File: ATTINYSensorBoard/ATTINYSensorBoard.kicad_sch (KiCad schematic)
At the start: 17 parts, among them J1 ICSP, J2 POWER/CAN, U1 ATtiny841-SS, U2 MCP25625-x-SS, U3 74HC04

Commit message: Finished Sensor Board Template
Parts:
- added J3: Conn_01x04, Connector_PinHeader_2.54mm:PinHeader_1x04_P2.54mm_Vertical, symbol Connector_Generic:Conn_01x04
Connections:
- net USER0: now also J3.1 (Pin_1)
- net USER1: now also J3.2 (Pin_2)
- net USER2: now also J3.3 (Pin_3)
- net USER3: now also J3.4 (Pin_4)
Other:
- company: Pack Motorsports Baja -> ©️ 2024 Pack Motorsports Baja
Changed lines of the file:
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@@
 	(title_block
 		(title "ATtiny Senor Board Template")
-		(date "2024-10-03")
+		(date "2024-10-17")
 		(rev "1")
-		(company "Pack Motorsports Baja")
-		(comment 1 "©️ 2024 Pack Motorsports")
+		(company "©️ 2024 Pack Motorsports Baja")
 	)
 	(junction
@@
 	(wire
 		(pts
-			(xy 127 88.9) (xy 127 71.12)
+			(xy 127 88.9) (xy 127 69.85)
 		)
 		(stroke
@@
 	(wire
 		(pts
-			(xy 125.73 68.58) (xy 125.73 86.36)
+			(xy 125.73 67.31) (xy 125.73 86.36)
 		)
 		(stroke
@@
 		)
 	)
+	(polyline
+		(pts
+			(xy 139.7 59.055) (xy 139.7 62.23)
+		)
+		(stroke
+			(width 0)
+			(type default)
+		)
+	)
 	(wire
 		(pts
@@
 		)
 	)
+	(polyline
+		(pts
+			(xy 136.525 59.055) (xy 139.7 59.055)
+		)
+		(stroke
+			(width 0)
+			(type default)
+		)
+	)
 	(wire
 		(pts
@@
 	(wire
 		(pts
-			(xy 128.27 73.66) (xy 134.62 73.66)
+			(xy 128.27 72.39) (xy 134.62 72.39)
 		)
 		(stroke
@@
 	(wire
 		(pts
-			(xy 125.73 68.58) (xy 134.62 68.58)
+			(xy 125.73 67.31) (xy 134.62 67.31)
 		)
 		(stroke
@@
 	(wire
 		(pts
-			(xy 127 71.12) (xy 134.62 71.12)
+			(xy 127 69.85) (xy 134.62 69.85)
 		)
 		(stroke
@@
 		)
 	)
-	(polyline
-		(pts
-			(xy 135.89 63.5) (xy 135.89 74.295)
-		)
-		(stroke
-			(width 0)
-			(type default)
-		)
-	)
 	(wire
 		(pts
@@
 	(wire
 		(pts
-			(xy 128.27 91.44) (xy 128.27 73.66)
+			(xy 128.27 91.44) (xy 128.27 72.39)
 		)
 		(stroke
@@
 		)
 	)
-	(polyline
-		(pts
-			(xy 134.62 63.5) (xy 135.89 63.5)
-		)
-		(stroke
-			(width 0)
-			(type default)
-		)
-	)
 	(wire
 		(pts
@@
 	(wire
 		(pts
-			(xy 124.46 66.04) (xy 124.46 83.82)
-		)
-		(stroke
-			(width 0)
-			(type default)
-		)
-	)
-	(polyline
-		(pts
-			(xy 134.62 74.295) (xy 135.89 74.295)
+			(xy 124.46 64.77) (xy 124.46 83.82)
 		)
 		(stroke
@@
 	(wire
 		(pts
-			(xy 124.46 66.04) (xy 134.62 66.04)
+			(xy 124.46 64.77) (xy 134.62 64.77)
 		)
 		(stroke
@@
 	(text "SENSOR\nINPUTS"
 		(exclude_from_sim no)
-		(at 136.398 69.088 0)
+		(at 128.27 59.182 0)
 		(effects
 			(font
@@
 	)
 	(label "USER2"
-		(at 134.62 71.12 180)
+		(at 134.62 69.85 180)
 		(fields_autoplaced yes)
 		(effects
@@
 	)
 	(label "USER3"
-		(at 134.62 73.66 180)
+		(at 134.62 72.39 180)
 		(fields_autoplaced yes)
 		(effects
@@
 	)
 	(label "USER0"
-		(at 134.62 66.04 180)
+		(at 134.62 64.77 180)
 		(fields_autoplaced yes)
 		(effects
@@
 	)
 	(label "USER1"
-		(at 134.62 68.58 180)
+		(at 134.62 67.31 180)
 		(fields_autoplaced yes)
 		(effects
@@
 					(unit 1)
 				)
+			)
+		)
+	)
+	(symbol
+		(lib_id "Connector_Generic:Conn_01x04")
+		(at 139.7 67.31 0)
+		(unit 1)
+		(exclude_from_sim no)
+		(in_bom yes)
+		(on_board yes)
+		(dnp no)
+		(fields_autoplaced yes)
+		(property "Reference" "J3"
+			(at 142.24 67.3099 0)
+			(effects
+				(font
+					(size 1.27 1.27)
+				)
+				(justify left)
+			)
+		)
+		(property "Value" "Conn_01x04"
+			(at 142.24 69.8499 0)
+			(effects
+				(font
+					(size 1.27 1.27)
+				)
+				(justify left)
+			)
+		)
+		(property "Footprint" "Connector_PinHeader_2.54mm:PinHeader_1x04_P2.54mm_Vertical"
+			(at 139.7 67.31 0)
+			(effects
+				(font
+					(size 1.27 1.27)
+				)
+				(hide yes)
+			)
+		)
+		(property "Datasheet" "~"
+			(at 139.7 67.31 0)
+			(effects
+				(font
+					(size 1.27 1.27)
+				)
+				(hide yes)
+			)
+		)
+		(property "Description" "Generic connector, single row, 01x04, script generated (kicad-library-utils/schlib/autogen/connector/)"
+			(at 139.7 67.31 0)
+			(effects
+				(font
+					(size 1.27 1.27)
+				)
+				(hide yes)
+			)
+		)
+		(pin "3"
+		)
+		(pin "4"
+		)
+		(pin "1"
+		)
+		(pin "2"
+		)
+		(instances
+			(project ""
+				(path "/6c2b8c5e-e617-4dcc-bfbe-6767b59298bb"
+					(reference "J3")
+					(unit 1)
+				)

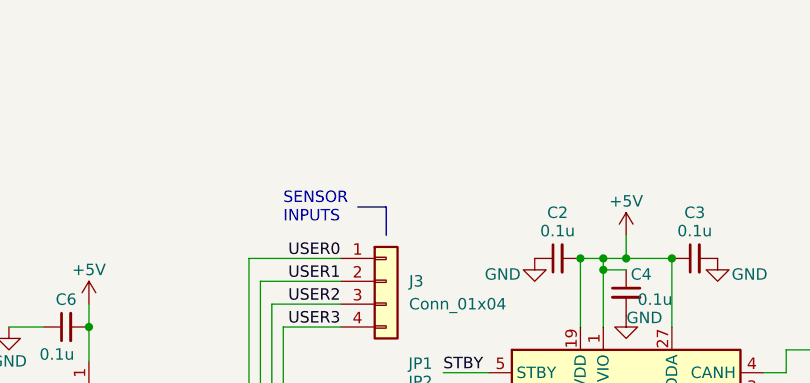
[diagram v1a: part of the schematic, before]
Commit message: Fixed grounds
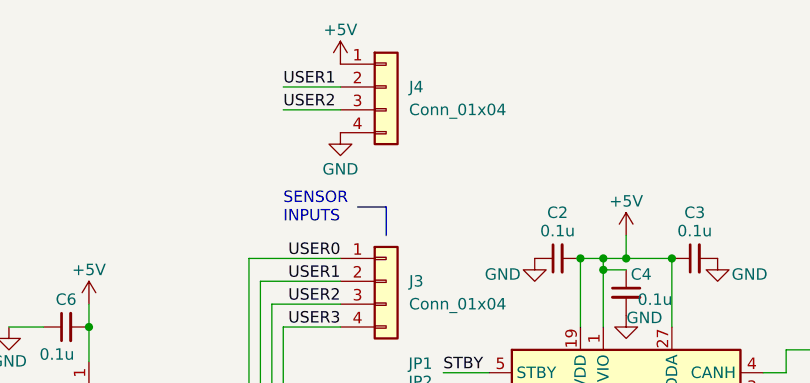
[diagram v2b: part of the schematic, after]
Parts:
- added J4: Conn_01x04, symbol Connector_Generic:Conn_01x04
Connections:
- net +5V: now also J4.1 (Pin_1)
- net GND: now also J4.4 (Pin_4)
- net USER1: now also J4.2 (Pin_2)
- net USER2: now also J4.3 (Pin_3)
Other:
- title: ATtiny Senor Board Template -> ATtiny Sensor Board Template
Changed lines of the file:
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@@
 	(paper "A4")
 	(title_block
-		(title "ATtiny Senor Board Template")
+		(title "ATtiny Sensor Board Template")
 		(date "2024-10-17")
 		(rev "1")
@@
 	(wire
 		(pts
+			(xy 128.27 48.26) (xy 134.62 48.26)
+		)
+		(stroke
+			(width 0)
+			(type default)
+		)
+	)
+	(wire
+		(pts
 			(xy 184.15 85.09) (xy 184.15 95.25)
 		)
@@
 	(wire
 		(pts
+			(xy 128.27 45.72) (xy 134.62 45.72)
+		)
+		(stroke
+			(width 0)
+			(type default)
+		)
+	)
+	(wire
+		(pts
 			(xy 134.62 96.52) (xy 121.92 96.52)
 		)
@@
 		)
 	)
+	(label "USER1"
+		(at 128.27 45.72 0)
+		(fields_autoplaced yes)
+		(effects
+			(font
+				(size 1.27 1.27)
+			)
+			(justify left bottom)
+		)
+	)
 	(label "STBY"
 		(at 146.05 77.47 0)
@@
 		)
 	)
+	(label "USER2"
+		(at 128.27 48.26 0)
+		(fields_autoplaced yes)
+		(effects
+			(font
+				(size 1.27 1.27)
+			)
+			(justify left bottom)
+		)
+	)
 	(symbol
 		(lib_id "power:PWR_FLAG")
@@
 	)
 	(symbol
+		(lib_id "power:+5V")
+		(at 134.62 43.18 0)
+		(unit 1)
+		(exclude_from_sim no)
+		(in_bom yes)
+		(on_board yes)
+		(dnp no)
+		(property "Reference" "#PWR025"
+			(at 134.62 46.99 0)
+			(effects
+				(font
+					(size 1.27 1.27)
+				)
+				(hide yes)
+			)
+		)
+		(property "Value" "+5V"
+			(at 134.62 39.37 0)
+			(effects
+				(font
+					(size 1.27 1.27)
+				)
+			)
+		)
+		(property "Footprint" ""
+			(at 134.62 43.18 0)
+			(effects
+				(font
+					(size 1.27 1.27)
+				)
+				(hide yes)
+			)
+		)
+		(property "Datasheet" ""
+			(at 134.62 43.18 0)
+			(effects
+				(font
+					(size 1.27 1.27)
+				)
+				(hide yes)
+			)
+		)
+		(property "Description" "Power symbol creates a global label with name \"+5V\""
+			(at 134.62 43.18 0)
+			(effects
+				(font
+					(size 1.27 1.27)
+				)
+				(hide yes)
+			)
+		)
+		(pin "1"
+		)
+		(instances
+			(project "ATTINYSensorBoard"
+				(path "/6c2b8c5e-e617-4dcc-bfbe-6767b59298bb"
+					(reference "#PWR025")
+					(unit 1)
+				)
+			)
+		)
+	)
+	(symbol
 		(lib_id "Device:C_Small")
 		(at 158.75 64.77 90)
@@
 	)
 	(symbol
+		(lib_id "power:GND")
+		(at 134.62 50.8 0)
+		(unit 1)
+		(exclude_from_sim no)
+		(in_bom yes)
+		(on_board yes)
+		(dnp no)
+		(property "Reference" "#PWR026"
+			(at 134.62 57.15 0)
+			(effects
+				(font
+					(size 1.27 1.27)
+				)
+				(hide yes)
+			)
+		)
+		(property "Value" "GND"
+			(at 134.62 54.864 0)
+			(effects
+				(font
+					(size 1.27 1.27)
+				)
+			)
+		)
+		(property "Footprint" ""
+			(at 134.62 50.8 0)
+			(effects
+				(font
+					(size 1.27 1.27)
+				)
+				(hide yes)
+			)
+		)
+		(property "Datasheet" ""
+			(at 134.62 50.8 0)
+			(effects
+				(font
+					(size 1.27 1.27)
+				)
+				(hide yes)
+			)
+		)
+		(property "Description" "Power symbol creates a global label with name \"GND\" , ground"
+			(at 134.62 50.8 0)
+			(effects
+				(font
+					(size 1.27 1.27)
+				)
+				(hide yes)
+			)
+		)
+		(pin "1"
+		)
+		(instances
+			(project "ATTINYSensorBoard"
+				(path "/6c2b8c5e-e617-4dcc-bfbe-6767b59298bb"
+					(reference "#PWR026")
+					(unit 1)
+				)
+			)
+		)
+	)
+	(symbol
 		(lib_id "power:+5V")
 		(at 166.37 62.23 0)
@@
 					(unit 1)
 				)
+			)
+		)
+	)
+	(symbol
+		(lib_id "Connector_Generic:Conn_01x04")
+		(at 139.7 45.72 0)
+		(unit 1)
+		(exclude_from_sim no)
+		(in_bom yes)
+		(on_board yes)
+		(dnp no)
+		(fields_autoplaced yes)
+		(property "Reference" "J4"
+			(at 142.24 45.7199 0)
+			(effects
+				(font
+					(size 1.27 1.27)
+				)
+				(justify left)
+			)
+		)
+		(property "Value" "Conn_01x04"
+			(at 142.24 48.2599 0)
+			(effects
+				(font
+					(size 1.27 1.27)
+				)
+				(justify left)
+			)
+		)
+		(property "Footprint" ""
+			(at 139.7 45.72 0)
+			(effects
+				(font
+					(size 1.27 1.27)
+				)
+				(hide yes)
+			)
+		)
+		(property "Datasheet" "~"
+			(at 139.7 45.72 0)
+			(effects
+				(font
+					(size 1.27 1.27)
+				)
+				(hide yes)
+			)
+		)
+		(property "Description" "Generic connector, single row, 01x04, script generated (kicad-library-utils/schlib/autogen/connector/)"
+			(at 139.7 45.72 0)
+			(effects
+				(font
+					(size 1.27 1.27)
+				)
+				(hide yes)
+			)
+		)
+		(pin "3"
+		)
+		(pin "1"
+		)
+		(pin "4"
+		)
+		(pin "2"
+		)
+		(instances
+			(project ""
+				(path "/6c2b8c5e-e617-4dcc-bfbe-6767b59298bb"
+					(reference "J4")
+					(unit 1)
+				)

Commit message: Pushing stuff
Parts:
- removed J4: Conn_01x04, symbol Connector_Generic:Conn_01x04
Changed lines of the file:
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@@
 	(wire
 		(pts
-			(xy 128.27 48.26) (xy 134.62 48.26)
-		)
-		(stroke
-			(width 0)
-			(type default)
-		)
-	)
-	(wire
-		(pts
 			(xy 184.15 85.09) (xy 184.15 95.25)
 		)
@@
 	(wire
 		(pts
-			(xy 128.27 45.72) (xy 134.62 45.72)
-		)
-		(stroke
-			(width 0)
-			(type default)
-		)
-	)
-	(wire
-		(pts
 			(xy 134.62 96.52) (xy 121.92 96.52)
 		)
@@
 		)
 	)
-	(label "USER1"
-		(at 128.27 45.72 0)
-		(fields_autoplaced yes)
-		(effects
-			(font
-				(size 1.27 1.27)
-			)
-			(justify left bottom)
-		)
-	)
 	(label "STBY"
 		(at 146.05 77.47 0)
@@
 		)
 	)
-	(label "USER2"
-		(at 128.27 48.26 0)
-		(fields_autoplaced yes)
-		(effects
-			(font
-				(size 1.27 1.27)
-			)
-			(justify left bottom)
-		)
-	)
 	(symbol
 		(lib_id "power:PWR_FLAG")
@@
 	)
 	(symbol
-		(lib_id "power:+5V")
-		(at 134.62 43.18 0)
-		(unit 1)
-		(exclude_from_sim no)
-		(in_bom yes)
-		(on_board yes)
-		(dnp no)
-		(property "Reference" "#PWR025"
-			(at 134.62 46.99 0)
-			(effects
-				(font
-					(size 1.27 1.27)
-				)
-				(hide yes)
-			)
-		)
-		(property "Value" "+5V"
-			(at 134.62 39.37 0)
-			(effects
-				(font
-					(size 1.27 1.27)
-				)
-			)
-		)
-		(property "Footprint" ""
-			(at 134.62 43.18 0)
-			(effects
-				(font
-					(size 1.27 1.27)
-				)
-				(hide yes)
-			)
-		)
-		(property "Datasheet" ""
-			(at 134.62 43.18 0)
-			(effects
-				(font
-					(size 1.27 1.27)
-				)
-				(hide yes)
-			)
-		)
-		(property "Description" "Power symbol creates a global label with name \"+5V\""
-			(at 134.62 43.18 0)
-			(effects
-				(font
-					(size 1.27 1.27)
-				)
-				(hide yes)
-			)
-		)
-		(pin "1"
-		)
-		(instances
-			(project "ATTINYSensorBoard"
-				(path "/6c2b8c5e-e617-4dcc-bfbe-6767b59298bb"
-					(reference "#PWR025")
-					(unit 1)
-				)
-			)
-		)
-	)
-	(symbol
 		(lib_id "Device:C_Small")
 		(at 158.75 64.77 90)
@@
 	)
 	(symbol
-		(lib_id "power:GND")
-		(at 134.62 50.8 0)
-		(unit 1)
-		(exclude_from_sim no)
-		(in_bom yes)
-		(on_board yes)
-		(dnp no)
-		(property "Reference" "#PWR026"
-			(at 134.62 57.15 0)
-			(effects
-				(font
-					(size 1.27 1.27)
-				)
-				(hide yes)
-			)
-		)
-		(property "Value" "GND"
-			(at 134.62 54.864 0)
-			(effects
-				(font
-					(size 1.27 1.27)
-				)
-			)
-		)
-		(property "Footprint" ""
-			(at 134.62 50.8 0)
-			(effects
-				(font
-					(size 1.27 1.27)
-				)
-				(hide yes)
-			)
-		)
-		(property "Datasheet" ""
-			(at 134.62 50.8 0)
-			(effects
-				(font
-					(size 1.27 1.27)
-				)
-				(hide yes)
-			)
-		)
-		(property "Description" "Power symbol creates a global label with name \"GND\" , ground"
-			(at 134.62 50.8 0)
-			(effects
-				(font
-					(size 1.27 1.27)
-				)
-				(hide yes)
-			)
-		)
-		(pin "1"
-		)
-		(instances
-			(project "ATTINYSensorBoard"
-				(path "/6c2b8c5e-e617-4dcc-bfbe-6767b59298bb"
-					(reference "#PWR026")
-					(unit 1)
-				)
-			)
-		)
-	)
-	(symbol
 		(lib_id "power:+5V")
 		(at 166.37 62.23 0)
@@
 					(unit 1)
 				)
-			)
-		)
-	)
-	(symbol
-		(lib_id "Connector_Generic:Conn_01x04")
-		(at 139.7 45.72 0)
-		(unit 1)
-		(exclude_from_sim no)
-		(in_bom yes)
-		(on_board yes)
-		(dnp no)
-		(fields_autoplaced yes)
-		(property "Reference" "J4"
-			(at 142.24 45.7199 0)
-			(effects
-				(font
-					(size 1.27 1.27)
-				)
-				(justify left)
-			)
-		)
-		(property "Value" "Conn_01x04"
-			(at 142.24 48.2599 0)
-			(effects
-				(font
-					(size 1.27 1.27)
-				)
-				(justify left)
-			)
-		)
-		(property "Footprint" ""
-			(at 139.7 45.72 0)
-			(effects
-				(font
-					(size 1.27 1.27)
-				)
-				(hide yes)
-			)
-		)
-		(property "Datasheet" "~"
-			(at 139.7 45.72 0)
-			(effects
-				(font
-					(size 1.27 1.27)
-				)
-				(hide yes)
-			)
-		)
-		(property "Description" "Generic connector, single row, 01x04, script generated (kicad-library-utils/schlib/autogen/connector/)"
-			(at 139.7 45.72 0)
-			(effects
-				(font
-					(size 1.27 1.27)
-				)
-				(hide yes)
-			)
-		)
-		(pin "3"
-		)
-		(pin "1"
-		)
-		(pin "4"
-		)
-		(pin "2"
-		)
-		(instances
-			(project ""
-				(path "/6c2b8c5e-e617-4dcc-bfbe-6767b59298bb"
-					(reference "J4")
-					(unit 1)
-				)
